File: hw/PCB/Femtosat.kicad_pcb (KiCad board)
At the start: 2 copper layers, 83.8 x 34 mm, 29 parts, among them J1 USB_B_Micro, J2 Programmer, J3 SMA, J4 Battery, U0 AP7215-33YG-13, U1 SAMD21G, U2 TRH-G2, U3 AV4524, U4 RFM69HCW, U5 XA1110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

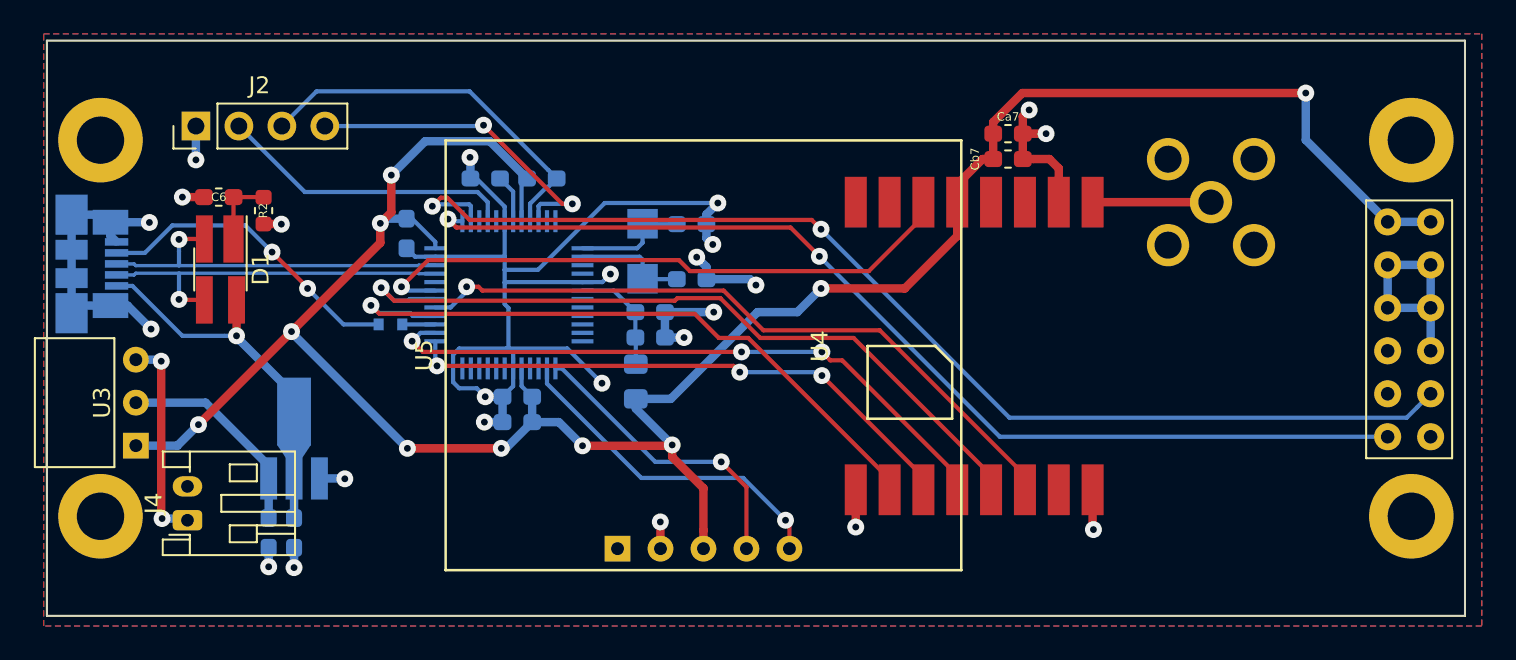
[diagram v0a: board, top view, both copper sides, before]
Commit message: Fixed error in which the GPS was in the top layer instead of the bottom layer. Version 1 released. Changed PCB's folder name to PCB.
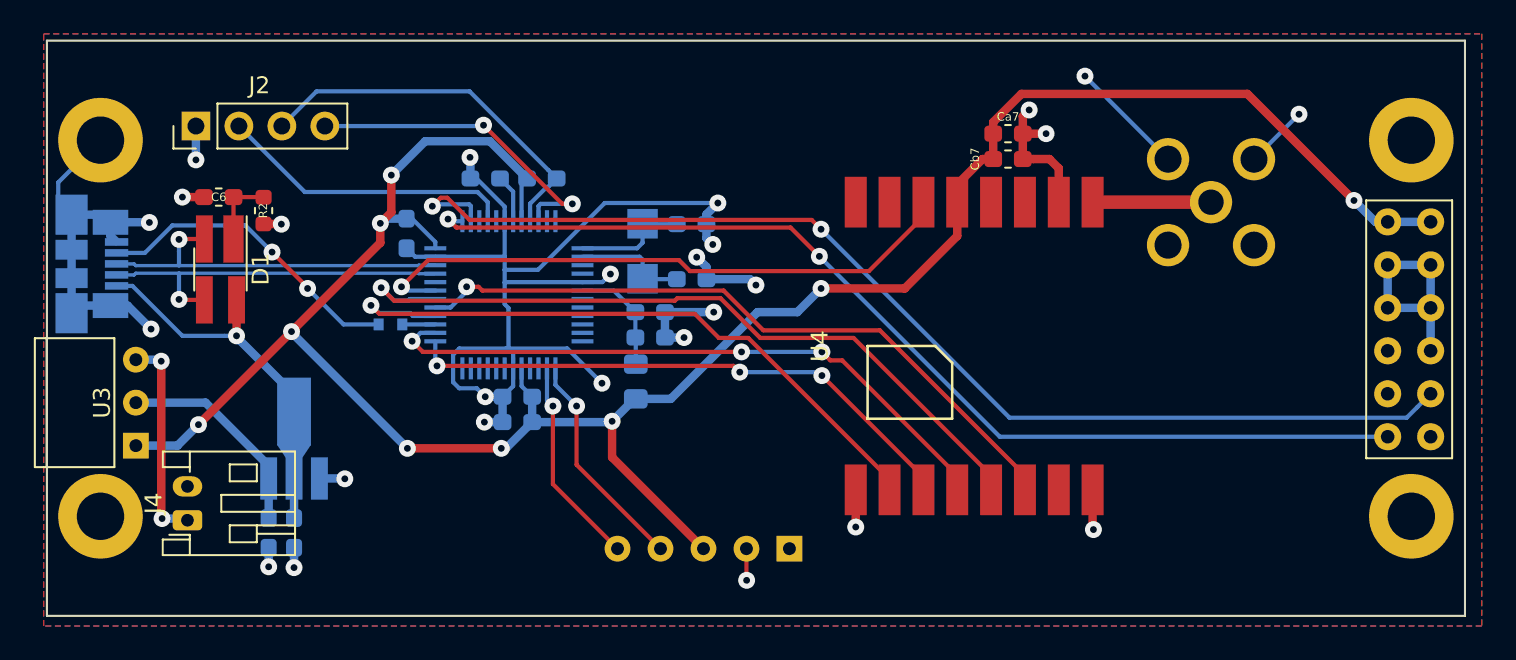
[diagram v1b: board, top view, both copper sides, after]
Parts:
- U5: moved to B.Cu
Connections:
- U2 pad : (no net) -> GND
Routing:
- net GND: track 125.9 -> 142.7 mm, vias 24 -> 26
- net /SCL: track 20.1 -> 12.4 mm
- net /SDA: track 17.8 -> 13.2 mm
- net /3V3: track 143.3 -> 138.7 mm, vias 10 -> 9
